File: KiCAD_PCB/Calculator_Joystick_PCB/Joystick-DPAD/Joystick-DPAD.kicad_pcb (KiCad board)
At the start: 2 copper layers, 40 x 60 mm, 9 parts, among them SW1 SW_SPST, SW2 SW_SPST, SW3 SW_SPST, SW4 SW_SPST

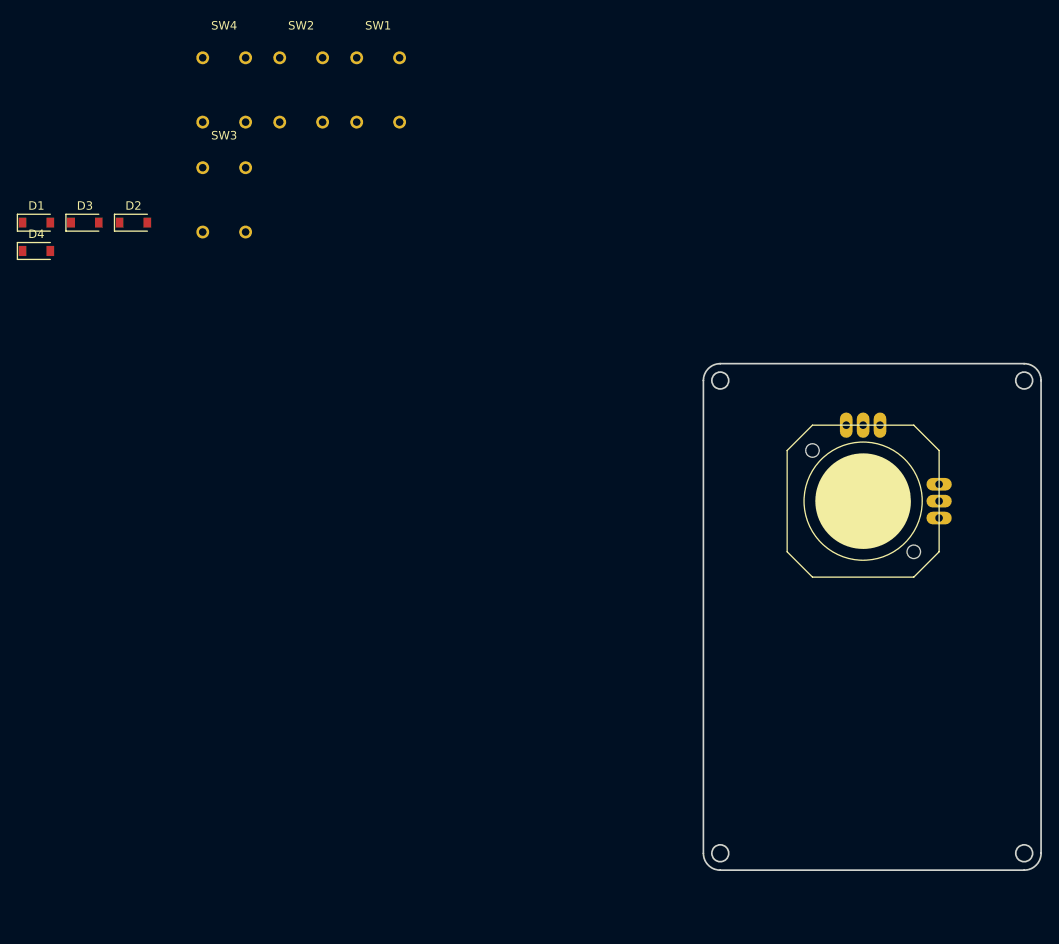
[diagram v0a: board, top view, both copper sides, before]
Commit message: JoyStick PCB Updates
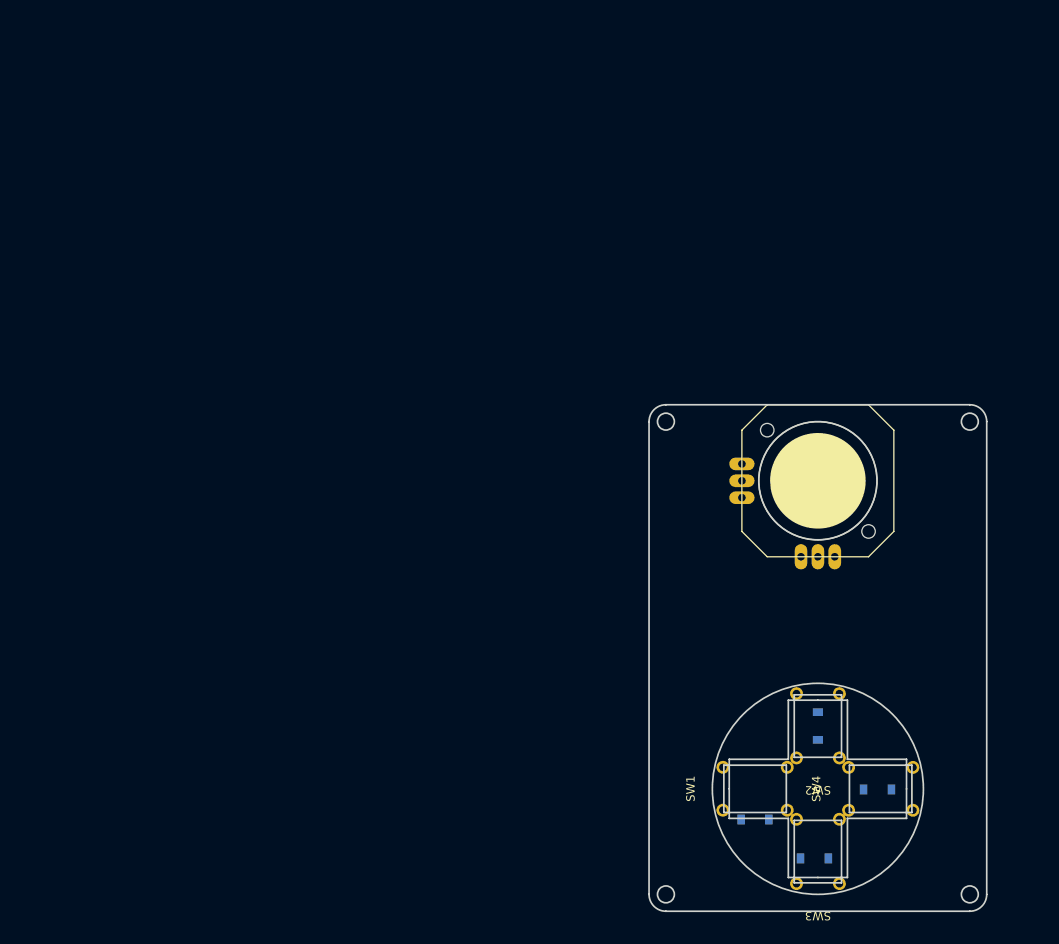
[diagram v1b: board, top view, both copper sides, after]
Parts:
- D1, D2, D3, D4: moved to B.Cu
- moved D4 118.3 mm to (150.1, 124.9), turned to 180 degrees
- moved D3 114.6 mm to (142.7, 133.1), turned to 180 degrees
- moved SW4 113.6 mm to (150.5, 124.8), turned to 90 degrees
- moved D1 110.7 mm to (135.6, 128.5)
- moved SW3 104.4 mm to (143.1, 132.3), turned to 180 degrees
- moved D2 100.6 mm to (143.1, 117.4), turned to 90 degrees
- moved SW2 97.1 mm to (143.1, 117.4), turned to 180 degrees
- moved SW1 94.1 mm to (135.6, 124.8), turned to 90 degrees
- moved JOY1 5.88 mm to (143.1, 88.3), turned to 180 degrees
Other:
- outline, holes or cut-outs redrawn

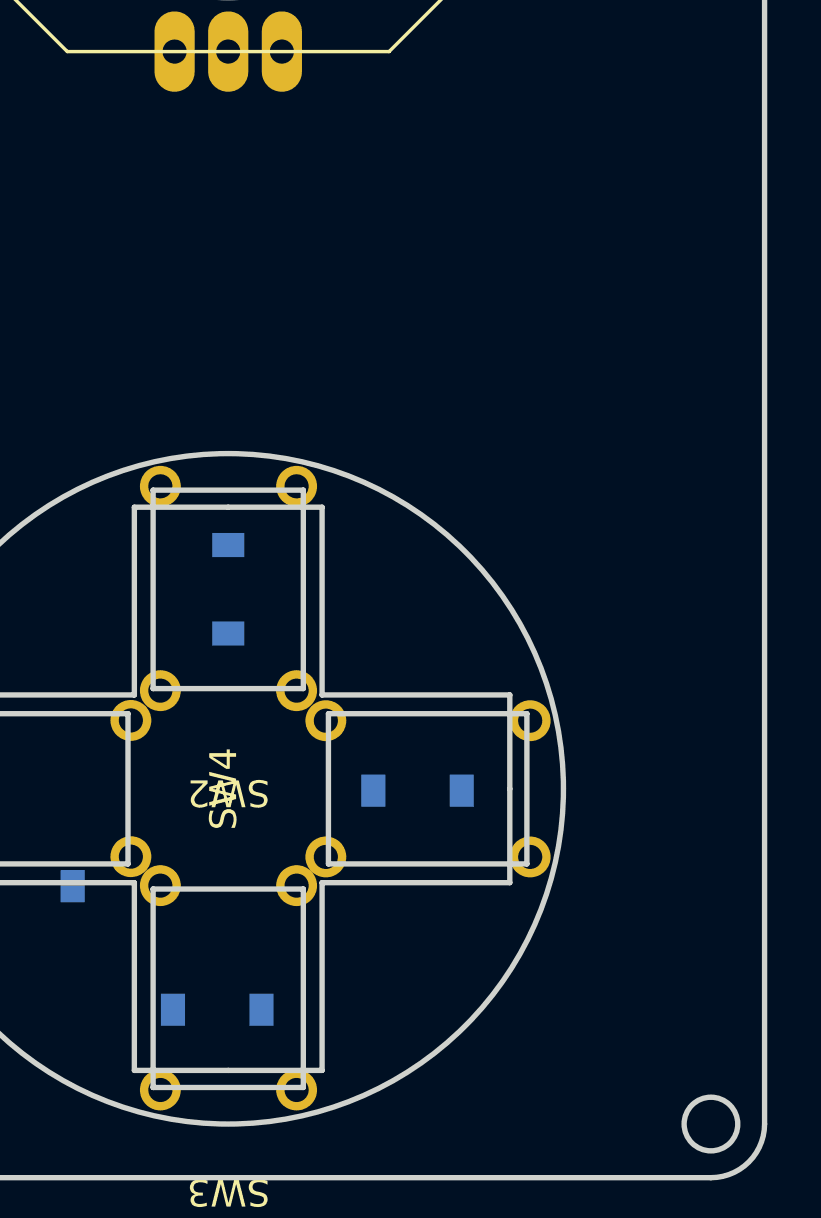
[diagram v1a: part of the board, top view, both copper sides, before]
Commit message: JoyStick PCB Updates
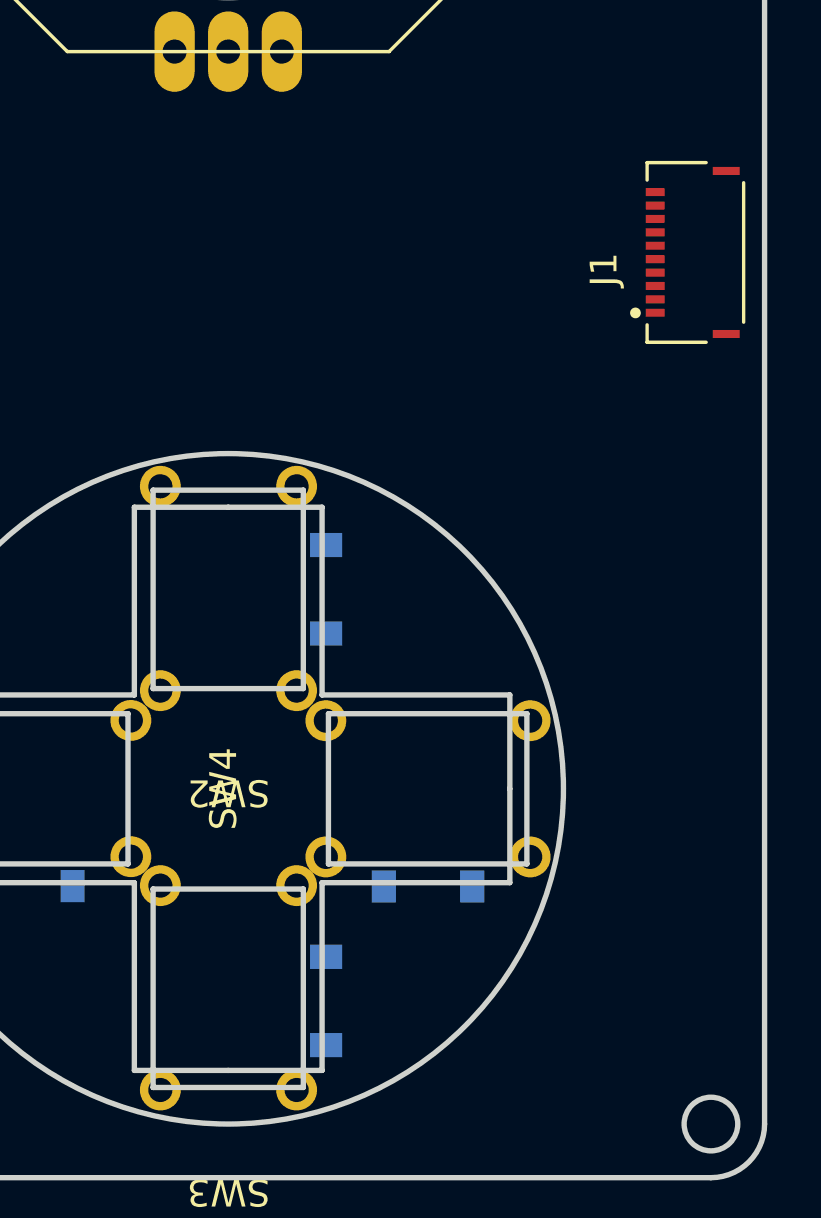
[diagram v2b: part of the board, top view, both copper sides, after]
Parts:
- added J1: 5034801000, 5034801000:MOLEX_5034801000, F.Cu at (159.0, 104.8)
- moved D3 4.07 mm to (146.7, 132.8), turned to 90 degrees
- moved D2 3.65 mm to (146.7, 117.4)
- moved D4 3.59 mm to (150.5, 128.5), turned to 0 degrees
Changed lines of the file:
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@@
   (net 12 "GND")
   (net 13 "/YOUT")
+  (net 14 "unconnected-(J1-Pad5)")
+  (net 15 "unconnected-(J1-Pad4)")
+  (net 16 "unconnected-(J1-Pad3)")
+  (net 17 "unconnected-(J1-Pad2)")
+  (net 18 "unconnected-(J1-Pad1)")
+  (net 19 "unconnected-(J1-Pad6)")
+  (net 20 "unconnected-(J1-Pad7)")
+  (net 21 "unconnected-(J1-Pad8)")
+  (net 22 "unconnected-(J1-Pad9)")
+  (net 23 "unconnected-(J1-Pad10)")
+  (net 24 "Net-(J1-PadS1)")
+  (footprint "5034801000:MOLEX_5034801000" (layer "F.Cu")
+    (at 158.99 104.84 90)
+    (property "MANUFACTURER" "MOLEX")
+    (property "PARTREV" "H")
+    (property "STANDARD" "Manufacturer Recommendation")
+    (property "Sheetfile" "Joystick-DPAD.kicad_sch")
+    (property "Sheetname" "")
+    (attr through_hole)
+    (fp_text reference "J1" (at -0.635 -1.905 90) (layer "F.SilkS")
+      (effects (font (size 1 1) (thickness 0.15)))
+    )
+    (fp_text value "5034801000" (at 6.35 4.445 90) (layer "F.Fab")
+      (effects (font (size 1 1) (thickness 0.15)))
+    )
+    (fp_line (start 2.7 -0.3) (end 3.35 -0.3) (layer "F.SilkS") (width 0.127))
+    (fp_line (start -2.7 -0.3) (end -3.35 -0.3) (layer "F.SilkS") (width 0.127))
+    (fp_line (start 3.35 -0.3) (end 3.35 1.9) (layer "F.SilkS") (width 0.127))
+    (fp_line (start -3.35 -0.3) (end -3.35 1.9) (layer "F.SilkS") (width 0.127))
+    (fp_line (start -2.6 3.3) (end 2.6 3.3) (layer "F.SilkS") (width 0.127))
+    (fp_circle (center -2.255 -0.735) (end -2.155 -0.735) (layer "F.SilkS") (width 0.2) (fill none))
+    (fp_line (start 3.6 3.55) (end -3.6 3.55) (layer "F.CrtYd") (width 0.05))
+    (fp_line (start -3.6 3.55) (end -3.6 -0.6) (layer "F.CrtYd") (width 0.05))
+    (fp_line (start -3.6 -0.6) (end 3.6 -0.6) (layer "F.CrtYd") (width 0.05))
+    (fp_line (start 3.6 -0.6) (end 3.6 3.55) (layer "F.CrtYd") (width 0.05))
+    (fp_line (start -3.35 3.3) (end -3.35 -0.3) (layer "F.Fab") (width 0.127))
+    (fp_line (start -3.35 -0.3) (end 3.35 -0.3) (layer "F.Fab") (width 0.127))
+    (fp_line (start 3.35 3.3) (end -3.35 3.3) (layer "F.Fab") (width 0.127))
+    (fp_line (start 3.35 -0.3) (end 3.35 3.3) (layer "F.Fab") (width 0.127))
+    (fp_circle (center -2.255 -0.735) (end -2.155 -0.735) (layer "F.Fab") (width 0.2) (fill none))
+    (pad "1" smd rect locked (at -2.25 0 90) (size 0.3 0.7) (layers "F.Cu" "F.Paste" "F.Mask")
+      (net 18 "unconnected-(J1-Pad1)") (pinfunction "1") (pintype "passive"))
+    (pad "2" smd rect locked (at -1.75 0 90) (size 0.3 0.7) (layers "F.Cu" "F.Paste" "F.Mask")
+      (net 17 "unconnected-(J1-Pad2)") (pinfunction "2") (pintype "passive"))
+    (pad "3" smd rect locked (at -1.25 0 90) (size 0.3 0.7) (layers "F.Cu" "F.Paste" "F.Mask")
+      (net 16 "unconnected-(J1-Pad3)") (pinfunction "3") (pintype "passive"))
+    (pad "4" smd rect locked (at -0.75 0 90) (size 0.3 0.7) (layers "F.Cu" "F.Paste" "F.Mask")
+      (net 15 "unconnected-(J1-Pad4)") (pinfunction "4") (pintype "passive"))
+    (pad "5" smd rect locked (at -0.25 0 90) (size 0.3 0.7) (layers "F.Cu" "F.Paste" "F.Mask")
+      (net 14 "unconnected-(J1-Pad5)") (pinfunction "5") (pintype "passive"))
+    (pad "6" smd rect locked (at 0.25 0 90) (size 0.3 0.7) (layers "F.Cu" "F.Paste" "F.Mask")
+      (net 19 "unconnected-(J1-Pad6)") (pinfunction "6") (pintype "passive"))
+    (pad "7" smd rect locked (at 0.75 0 90) (size 0.3 0.7) (layers "F.Cu" "F.Paste" "F.Mask")
+      (net 20 "unconnected-(J1-Pad7)") (pinfunction "7") (pintype "passive"))
+    (pad "8" smd rect locked (at 1.25 0 90) (size 0.3 0.7) (layers "F.Cu" "F.Paste" "F.Mask")
+      (net 21 "unconnected-(J1-Pad8)") (pinfunction "8") (pintype "passive"))
+    (pad "9" smd rect locked (at 1.75 0 90) (size 0.3 0.7) (layers "F.Cu" "F.Paste" "F.Mask")
+      (net 22 "unconnected-(J1-Pad9)") (pinfunction "9") (pintype "passive"))
+    (pad "10" smd rect locked (at 2.25 0 90) (size 0.3 0.7) (layers "F.Cu" "F.Paste" "F.Mask")
+      (net 23 "unconnected-(J1-Pad10)") (pinfunction "10") (pintype "passive"))
+    (pad "S1" smd rect locked (at -3.04 2.65 90) (size 0.3 1) (layers "F.Cu" "F.Paste" "F.Mask")
+      (net 24 "Net-(J1-PadS1)") (pinfunction "SHIELD") (pintype "passive"))
+    (pad "S2" smd rect locked (at 3.04 2.65 90) (size 0.3 1) (layers "F.Cu" "F.Paste" "F.Mask")
+      (net 24 "Net-(J1-PadS1)") (pinfunction "SHIELD") (pintype "passive"))
+  )
   (footprint "Adafruit_Thumbstick:JOYSTICK_ANALOG_MINITHM" (layer "F.Cu")
     (at 143.07 88.35 180)
@@
   )
   (footprint "Diode_SMD:D_SOD-123" (layer "B.Cu")
-    (at 142.66 133.08 180)
+    (at 146.72 132.75 90)
     (descr "SOD-123")
     (tags "SOD-123")
@@
     (property "Sheetname" "")
     (attr smd)
-    (fp_text reference "D3" (at 0 2) (layer "B.SilkS")
-      (effects (font (size 1 1) (thickness 0.15)) (justify mirror))
-    )
-    (fp_text value "D_Small" (at 0 -2.1) (layer "B.Fab")
-      (effects (font (size 1 1) (thickness 0.15)) (justify mirror))
-    )
-    (fp_text user "${REFERENCE}" (at 0 2) (layer "B.Fab")
+    (fp_text reference "D3" (at 0 2 90) (layer "B.SilkS")
+      (effects (font (size 1 1) (thickness 0.15)) (justify mirror))
+    )
+    (fp_text value "D_Small" (at 0 -2.1 90) (layer "B.Fab")
+      (effects (font (size 1 1) (thickness 0.15)) (justify mirror))
+    )
+    (fp_text user "${REFERENCE}" (at 0 2 90) (layer "B.Fab")
       (effects (font (size 1 1) (thickness 0.15)) (justify mirror))
     )
@@
     (fp_line (start -0.35 0) (end 0.25 0.4) (layer "B.Fab") (width 0.1))
     (fp_line (start -1.4 -0.9) (end -1.4 0.9) (layer "B.Fab") (width 0.1))
-    (pad "1" smd rect (at -1.65 0 180) (size 0.9 1.2) (layers "B.Cu" "B.Paste" "B.Mask")
+    (pad "1" smd rect (at -1.65 0 90) (size 0.9 1.2) (layers "B.Cu" "B.Paste" "B.Mask")
       (net 1 "/Row2") (pinfunction "K") (pintype "passive"))
-    (pad "2" smd rect (at 1.65 0 180) (size 0.9 1.2) (layers "B.Cu" "B.Paste" "B.Mask")
+    (pad "2" smd rect (at 1.65 0 90) (size 0.9 1.2) (layers "B.Cu" "B.Paste" "B.Mask")
       (net 5 "Net-(D3-Pad2)") (pinfunction "A") (pintype "passive"))
     (model "${KICAD6_3DMODEL_DIR}/Diode_SMD.3dshapes/D_SOD-123.wrl"
@@
   )
   (footprint "Diode_SMD:D_SOD-123" (layer "B.Cu")
-    (at 143.07 117.4 90)
+    (at 146.72 117.4 90)
     (descr "SOD-123")
     (tags "SOD-123")
@@
   )
   (footprint "Diode_SMD:D_SOD-123" (layer "B.Cu")
-    (at 150.13 124.91 180)
+    (at 150.52 128.48)
     (descr "SOD-123")
     (tags "SOD-123")
@@
     (fp_line (start 0.25 -0.4) (end -0.35 0) (layer "B.Fab") (width 0.1))
     (fp_line (start -0.35 0) (end -0.35 0.55) (layer "B.Fab") (width 0.1))
-    (pad "1" smd rect (at -1.65 0 180) (size 0.9 1.2) (layers "B.Cu" "B.Paste" "B.Mask")
+    (pad "1" smd rect (at -1.65 0) (size 0.9 1.2) (layers "B.Cu" "B.Paste" "B.Mask")
       (net 1 "/Row2") (pinfunction "K") (pintype "passive"))
-    (pad "2" smd rect (at 1.65 0 180) (size 0.9 1.2) (layers "B.Cu" "B.Paste" "B.Mask")
+    (pad "2" smd rect (at 1.65 0) (size 0.9 1.2) (layers "B.Cu" "B.Paste" "B.Mask")
       (net 6 "Net-(D4-Pad2)") (pinfunction "A") (pintype "passive"))
     (model "${KICAD6_3DMODEL_DIR}/Diode_SMD.3dshapes/D_SOD-123.wrl"

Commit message: V2 Updates
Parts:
- added JP1: , Adafruit Mini Analog Thumbstick:1X04_ROUND_76, F.Cu at (156.2, 89.6)
- J1: moved to B.Cu
- moved J1 12.4 mm to (161.8, 116.9), turned to -90 degrees
- moved D2 0.50 mm to (147.1, 117.0)
- moved D4 0.50 mm to (150.9, 128.8)
- moved D1 0.49 mm to (135.3, 128.8)
- moved D3 0.38 mm to (147.1, 132.6)
- moved SW3 0.36 mm to (143.1, 132.6)
- moved SW1 0.34 mm to (135.3, 124.8)
- moved SW4 0.34 mm to (150.9, 124.8)
- moved SW2 0.32 mm to (143.1, 117.0)
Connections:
- J1 pad 1: unconnected-(J1-Pad1) -> /y_out
- J1 pad 2: unconnected-(J1-Pad2) -> /x_out
- J1 pad 3: unconnected-(J1-Pad3) -> /Col2
- J1 pad 4: unconnected-(J1-Pad4) -> /Col1
- J1 pad 5: unconnected-(J1-Pad5) -> /Col0
- J1 pad 6: unconnected-(J1-Pad6) -> /Row3
- J1 pad 7: unconnected-(J1-Pad7) -> /Row4
- J1 pad 8: unconnected-(J1-Pad8) -> /Row5
- J1 pad S1: Net-(J1-PadS1) -> GND
- J1 pad S2: Net-(J1-PadS1) -> GND
- JOY1 pad X: /XOUT -> /x_out
- JOY1 pad Y: /YOUT -> /y_out
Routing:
- net /y_out: track 0.00 -> 51.4 mm
- net /x_out: track 0.00 -> 43.8 mm
- net 3.3V: track 0.00 -> 42.8 mm
- net GND: track 0.00 -> 34.1 mm
- net /Col1: track 0.00 -> 18.4 mm
- net Net-(D3-Pad2): track 0.00 -> 3.55 mm
- net Net-(D2-Pad2): track 0.00 -> 3.55 mm
- net Net-(D4-Pad2): track 0.00 -> 3.55 mm
- net Net-(D1-Pad2): track 0.00 -> 3.55 mm
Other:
- board size 40 x 60 mm -> 45 x 60 mm

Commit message: V2 Updates
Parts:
- added REF**: MountingHole_2.2mm_M2_DIN965, MountingHole:MountingHole_2.2mm_M2_DIN965, F.Cu at (163.6, 81.3)
- added REF**: MountingHole_2.2mm_M2_DIN965, MountingHole:MountingHole_2.2mm_M2_DIN965, F.Cu at (163.6, 137.3)
- added REF**: MountingHole_2.2mm_M2_DIN965, MountingHole:MountingHole_2.2mm_M2_DIN965, F.Cu at (122.6, 81.3)
- added REF**: MountingHole_2.2mm_M2_DIN965, MountingHole:MountingHole_2.2mm_M2_DIN965, F.Cu at (122.6, 137.3)
- added REF**: PinHeader_1x01_P2.00mm_Vertical, Connector_PinHeader_2.00mm:PinHeader_1x01_P2.00mm_Vertical, B.Cu at (128.0, 81.5)
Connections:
- D1 pad 1: /Row2 -> /Row4
- D2 pad 1: /Row1 -> /Row3
- D3 pad 1: /Row2 -> /Row5
- D4 pad 1: /Row2 -> /Row4
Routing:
- net /Col1: track 18.4 -> 84.5 mm
- net /Row4: track 0.00 -> 39.1 mm
- net /Col0: track 0.00 -> 29.7 mm
- net /Row5: track 0.00 -> 25.6 mm
- net /Col2: track 0.00 -> 21.9 mm
- net /Row3: track 0.00 -> 15.4 mm, vias 0 -> 2
- net GND: track 34.1 -> 38.4 mm, vias 0 -> 2
- added copper zone on F.Cu, net GND
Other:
- outline, holes or cut-outs redrawn
